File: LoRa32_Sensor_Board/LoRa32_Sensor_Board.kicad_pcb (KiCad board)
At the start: 2 copper layers, 82.6 x 94 mm, 19 parts, among them J1 Battery holder, U1 LSM303C, U2 TTGO_LoRa32, U3 MPL115A1, U4 ublox_SAM-M8Q, U5 STC3100

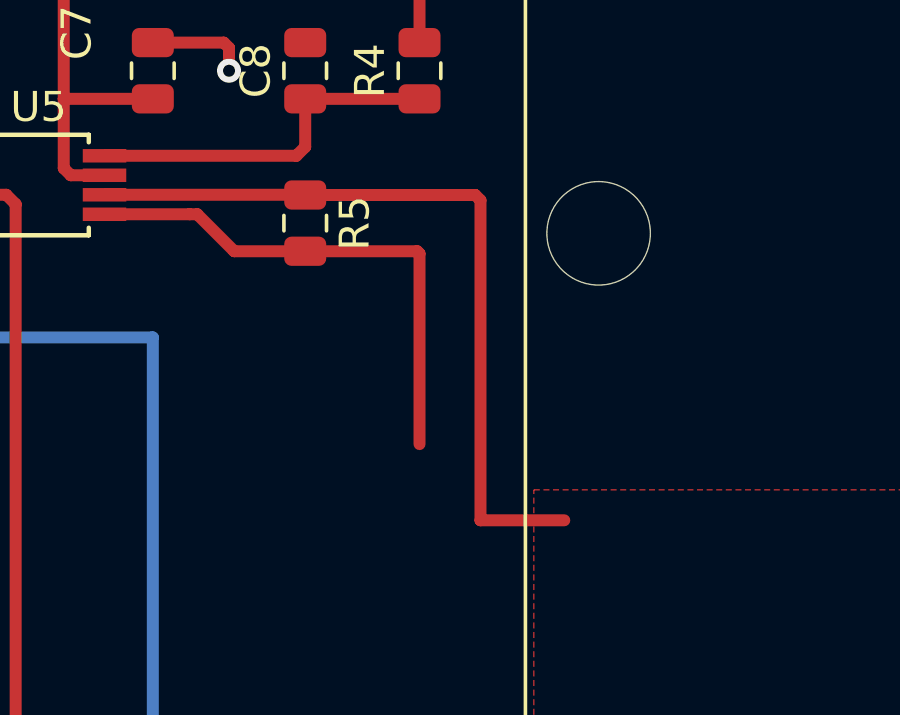
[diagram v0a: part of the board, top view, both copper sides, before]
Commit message: README.md for the hardware part added, sense resistor tracks widened
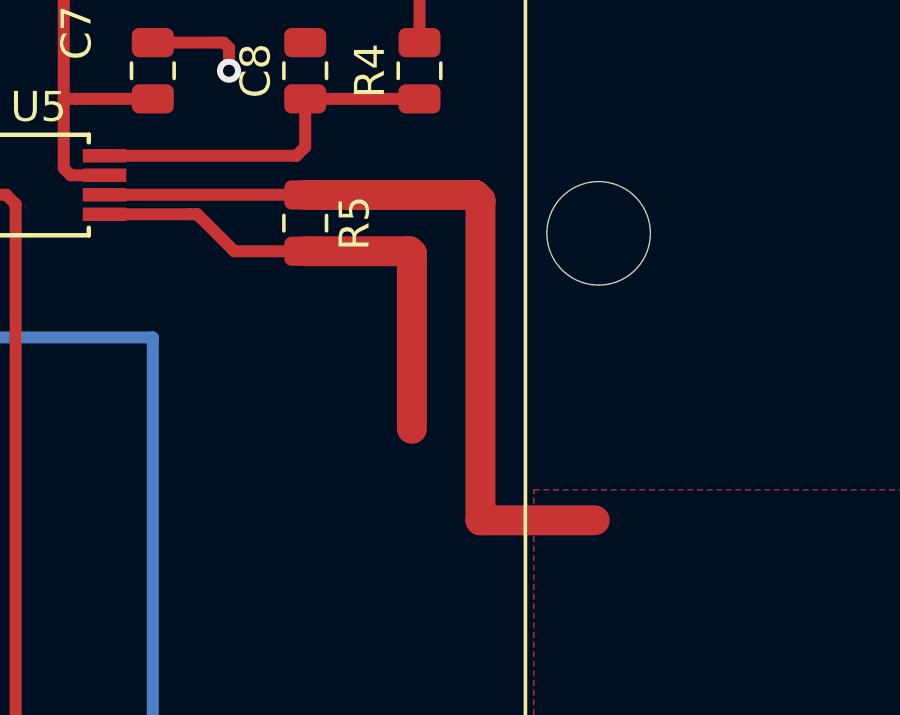
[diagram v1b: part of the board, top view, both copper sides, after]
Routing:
- net -BATT: track 26.1 -> 27.1 mm
- net GND: track 23.2 -> 22.5 mm
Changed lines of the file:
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@@
   (segment (start 200.8355 55.5475) (end 199.603 54.315) (width 0.4) (layer F.Cu) (net 3))
   (segment (start 203.2 55.5475) (end 200.8355 55.5475) (width 0.4) (layer F.Cu) (net 3))
-  (segment (start 203.2 55.5475) (end 206.9315 55.5475) (width 0.4) (layer F.Cu) (net 3))
-  (segment (start 206.9315 55.5475) (end 207.01 55.626) (width 0.4) (layer F.Cu) (net 3))
-  (segment (start 207.01 55.626) (end 207.01 61.976) (width 0.4) (layer F.Cu) (net 3))
   (segment (start 198.12 48.5925) (end 200.4845 48.5925) (width 0.4) (layer F.Cu) (net 3))
   (via (at 200.66 49.53) (size 0.8) (drill 0.4) (layers F.Cu B.Cu) (net 3))
@@
   (segment (start 192.7825 83.8325) (end 192.7825 84.5785) (width 0.2) (layer F.Cu) (net 3))
   (segment (start 192.7825 84.5785) (end 193.294 85.09) (width 0.2) (layer F.Cu) (net 3))
+  (segment (start 203.2 55.5475) (end 206.6775 55.5475) (width 1) (layer F.Cu) (net 3))
+  (segment (start 206.6775 55.5475) (end 206.756 55.626) (width 1) (layer F.Cu) (net 3))
+  (segment (start 206.756 55.626) (end 206.756 61.468) (width 1) (layer F.Cu) (net 3))
   (segment (start 192.11 53.015) (end 189.413 53.015) (width 0.4) (layer F.Cu) (net 4))
   (segment (start 189.23 52.832) (end 189.23 50.4675) (width 0.4) (layer F.Cu) (net 4))
@@
   (segment (start 162.1305 97.4575) (end 163.83 97.4575) (width 0.4) (layer F.Cu) (net 6))
   (segment (start 161.676 97.912) (end 162.1305 97.4575) (width 0.4) (layer F.Cu) (net 6))
-  (segment (start 167.835 100.935) (end 168.753 100.935) (width 0.4) (layer F.Cu) (net 47))
-  (segment (start 168.753 100.935) (end 168.91 101.092) (width 0.4) (layer F.Cu) (net 47))
-  (segment (start 168.91 101.092) (end 168.91 102.362) (width 0.4) (layer F.Cu) (net 47))
-  (segment (start 168.91 102.362) (end 181.61 102.362) (width 0.4) (layer F.Cu) (net 47))
-  (segment (start 181.61 102.362) (end 181.61 98.7275) (width 0.4) (layer F.Cu) (net 47))
   (segment (start 203.1925 53.665) (end 203.2 53.6725) (width 0.4) (layer F.Cu) (net 7))
   (segment (start 196.51 53.665) (end 203.1925 53.665) (width 0.4) (layer F.Cu) (net 7))
-  (segment (start 203.2 53.6725) (end 208.8665 53.6725) (width 0.4) (layer F.Cu) (net 7))
-  (segment (start 208.8665 53.6725) (end 209.042 53.848) (width 0.4) (layer F.Cu) (net 7))
-  (segment (start 209.042 53.848) (end 209.042 64.516) (width 0.4) (layer F.Cu) (net 7))
-  (segment (start 209.042 64.516) (end 211.836 64.516) (width 0.4) (layer F.Cu) (net 7))
+  (segment (start 203.2 53.6725) (end 208.8665 53.6725) (width 1) (layer F.Cu) (net 7))
+  (segment (start 208.8665 53.6725) (end 209.042 53.848) (width 1) (layer F.Cu) (net 7))
+  (segment (start 209.042 53.848) (end 209.042 64.516) (width 1) (layer F.Cu) (net 7))
+  (segment (start 209.042 64.516) (end 212.852 64.516) (width 1) (layer F.Cu) (net 7))
   (via (at 198.12 88.9) (size 0.8) (drill 0.4) (layers F.Cu B.Cu) (net 12))
   (segment (start 198.12 107.7) (end 198.12 88.9) (width 0.4) (layer F.Cu) (net 12))
@@
   (segment (start 172.603 99.685) (end 172.72 99.568) (width 0.4) (layer F.Cu) (net 46))
   (segment (start 169.985 99.685) (end 172.603 99.685) (width 0.4) (layer F.Cu) (net 46))
+  (segment (start 167.835 100.935) (end 168.753 100.935) (width 0.4) (layer F.Cu) (net 47))
+  (segment (start 168.753 100.935) (end 168.91 101.092) (width 0.4) (layer F.Cu) (net 47))
+  (segment (start 168.91 101.092) (end 168.91 102.362) (width 0.4) (layer F.Cu) (net 47))
+  (segment (start 168.91 102.362) (end 181.61 102.362) (width 0.4) (layer F.Cu) (net 47))
+  (segment (start 181.61 102.362) (end 181.61 98.7275) (width 0.4) (layer F.Cu) (net 47))
   (segment (start 181.542081 78.74) (end 184.404 81.601919) (width 0.4) (layer F.Cu) (net 47))
   (segment (start 180.34 78.74) (end 181.542081 78.74) (width 0.4) (layer F.Cu) (net 47))

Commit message: DRDY_MAG, INT_XL and INT_MAG pins from LSM303C connected to ESP32
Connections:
- U1 pad 11: Net-(U1-Pad11) -> /DRDY_MAG
- U1 pad 12: Net-(U1-Pad12) -> /INT_XL
- U1 pad 7: Net-(U1-Pad7) -> /INT_MAG
- U2 pad 16: Net-(U2-Pad16) -> /INT_MAG
- U2 pad 17: Net-(U2-Pad17) -> /INT_XL
- U2 pad 9: Net-(U2-Pad9) -> /DRDY_MAG
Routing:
- net /DRDY_MAG: track 0.00 -> 67.8 mm, vias 0 -> 2
- net /INT_MAG: track 0.00 -> 49.8 mm, vias 0 -> 2
- net /INT_XL: track 0.00 -> 40.6 mm, vias 0 -> 2

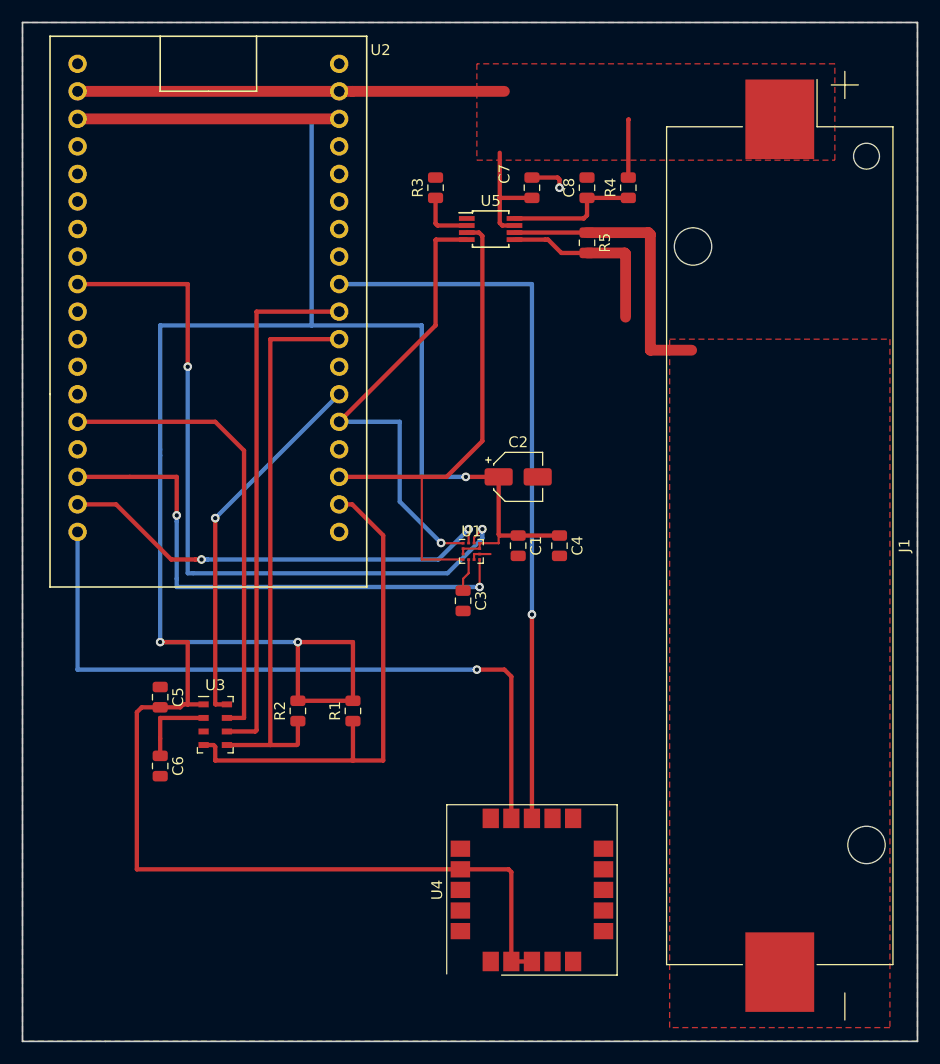
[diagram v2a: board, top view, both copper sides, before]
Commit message: Add LIS3MDL sensor project, add mounting holes to board
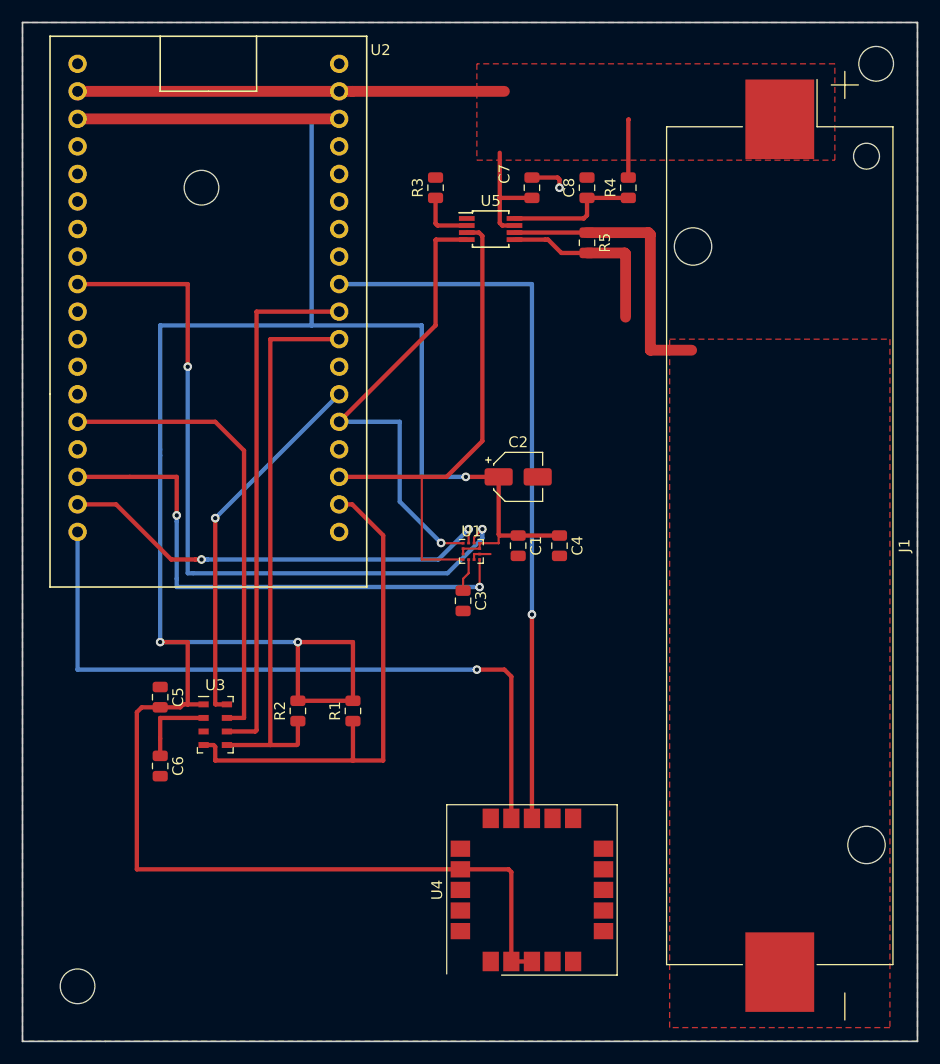
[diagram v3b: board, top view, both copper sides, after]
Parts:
- added REF**: MountingHole_3.2mm_M3_DIN965, MountingHole:MountingHole_3.2mm_M3_DIN965, F.Cu at (229.9, 38.1)
- added REF**: MountingHole_3.2mm_M3_DIN965, MountingHole:MountingHole_3.2mm_M3_DIN965, F.Cu at (156.2, 123.2)
- added REF**: MountingHole_3.2mm_M3_DIN965, MountingHole:MountingHole_3.2mm_M3_DIN965, F.Cu at (167.6, 49.5)
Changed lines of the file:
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@@
     (tracks 176)
     (zones 0)
-    (modules 19)
+    (modules 22)
     (nets 45)
   )
   (page A4)
+  (title_block
+    (title "LoRa32 Sensor Board")
+    (date 2019-04-08)
+    (rev 1)
+    (company "Pablo Maiolo")
+  )
   (layers
     (0 F.Cu signal)
@@
     (mod_text_size 1 1)
     (mod_text_width 0.15)
-    (pad_size 1.524 1.524)
-    (pad_drill 0.762)
+    (pad_size 3.2 3.2)
+    (pad_drill 3.2)
     (pad_to_mask_clearance 0.051)
     (solder_mask_min_width 0.25)
@@
     )
   )
+  (module MountingHole:MountingHole_3.2mm_M3_DIN965 (layer F.Cu)
+    (at 229.87 38.1)
+    (descr "Mounting Hole 3.2mm, no annular, M3, DIN965")
+    (tags "mounting hole 3.2mm no annular m3 din965")
+    (zone_connect 2)
+    (attr virtual)
+    (fp_text reference REF** (at 0 -3.8) (layer F.SilkS) hide
+      (effects (font (size 1 1) (thickness 0.15)))
+    )
+    (fp_text value MountingHole_3.2mm_M3_DIN965 (at 0 3.8) (layer F.Fab)
+      (effects (font (size 1 1) (thickness 0.15)))
+    )
+    (fp_circle (center 0 0) (end 3.05 0) (layer F.CrtYd) (width 0.05))
+    (fp_circle (center 0 0) (end 2.8 0) (layer Cmts.User) (width 0.15))
+    (fp_text user %R (at 0.3 0) (layer F.Fab)
+      (effects (font (size 1 1) (thickness 0.15)))
+    )
+    (pad 1 np_thru_hole circle (at 0 0) (size 3.2 3.2) (drill 3.2) (layers *.Cu *.Mask)
+      (zone_connect 2))
+  )
+  (module MountingHole:MountingHole_3.2mm_M3_DIN965 (layer F.Cu)
+    (at 156.21 123.19)
+    (descr "Mounting Hole 3.2mm, no annular, M3, DIN965")
+    (tags "mounting hole 3.2mm no annular m3 din965")
+    (zone_connect 2)
+    (attr virtual)
+    (fp_text reference REF** (at 0 -3.8) (layer F.SilkS) hide
+      (effects (font (size 1 1) (thickness 0.15)))
+    )
+    (fp_text value MountingHole_3.2mm_M3_DIN965 (at 0 3.8) (layer F.Fab)
+      (effects (font (size 1 1) (thickness 0.15)))
+    )
+    (fp_circle (center 0 0) (end 3.05 0) (layer F.CrtYd) (width 0.05))
+    (fp_circle (center 0 0) (end 2.8 0) (layer Cmts.User) (width 0.15))
+    (fp_text user %R (at 0.3 0) (layer F.Fab)
+      (effects (font (size 1 1) (thickness 0.15)))
+    )
+    (pad "" np_thru_hole circle (at 0 0) (size 3.2 3.2) (drill 3.2) (layers *.Cu *.Mask)
+      (zone_connect 2))
+  )
+  (module MountingHole:MountingHole_3.2mm_M3_DIN965 (layer F.Cu)
+    (at 167.64 49.53)
+    (descr "Mounting Hole 3.2mm, no annular, M3, DIN965")
+    (tags "mounting hole 3.2mm no annular m3 din965")
+    (zone_connect 2)
+    (attr virtual)
+    (fp_text reference REF** (at 0 -3.8) (layer F.SilkS) hide
+      (effects (font (size 1 1) (thickness 0.15)))
+    )
+    (fp_text value MountingHole_3.2mm_M3_DIN965 (at 0 3.8) (layer F.Fab)
+      (effects (font (size 1 1) (thickness 0.15)))
+    )
+    (fp_circle (center 0 0) (end 3.05 0) (layer F.CrtYd) (width 0.05))
+    (fp_circle (center 0 0) (end 2.8 0) (layer Cmts.User) (width 0.15))
+    (fp_text user %R (at 0.3 0) (layer F.Fab)
+      (effects (font (size 1 1) (thickness 0.15)))
+    )
+    (pad 1 np_thru_hole circle (at 0 0) (size 3.2 3.2) (drill 3.2) (layers *.Cu *.Mask)
+      (zone_connect 2))
+  )
   (gr_line (start 151.13 128.27) (end 158.75 128.27) (layer Edge.Cuts) (width 0.15))
